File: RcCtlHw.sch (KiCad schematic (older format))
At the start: 28 parts, among them J1 USB_B_Mini, J2 Program, J3 TFT_LCD, SW1 On/Off, U1 TP4056, U2 ESP-M2, U3 ADS1015, U4 Joystick

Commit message: 2nd attempt, looking good
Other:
- note added: "Move SW other side of reg"
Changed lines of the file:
@@
 	1    0    0    -1
 $EndComp
+Text Notes 2300 4650 0    50   ~ 0
+Move SW other side of reg
 $EndSCHEMATC

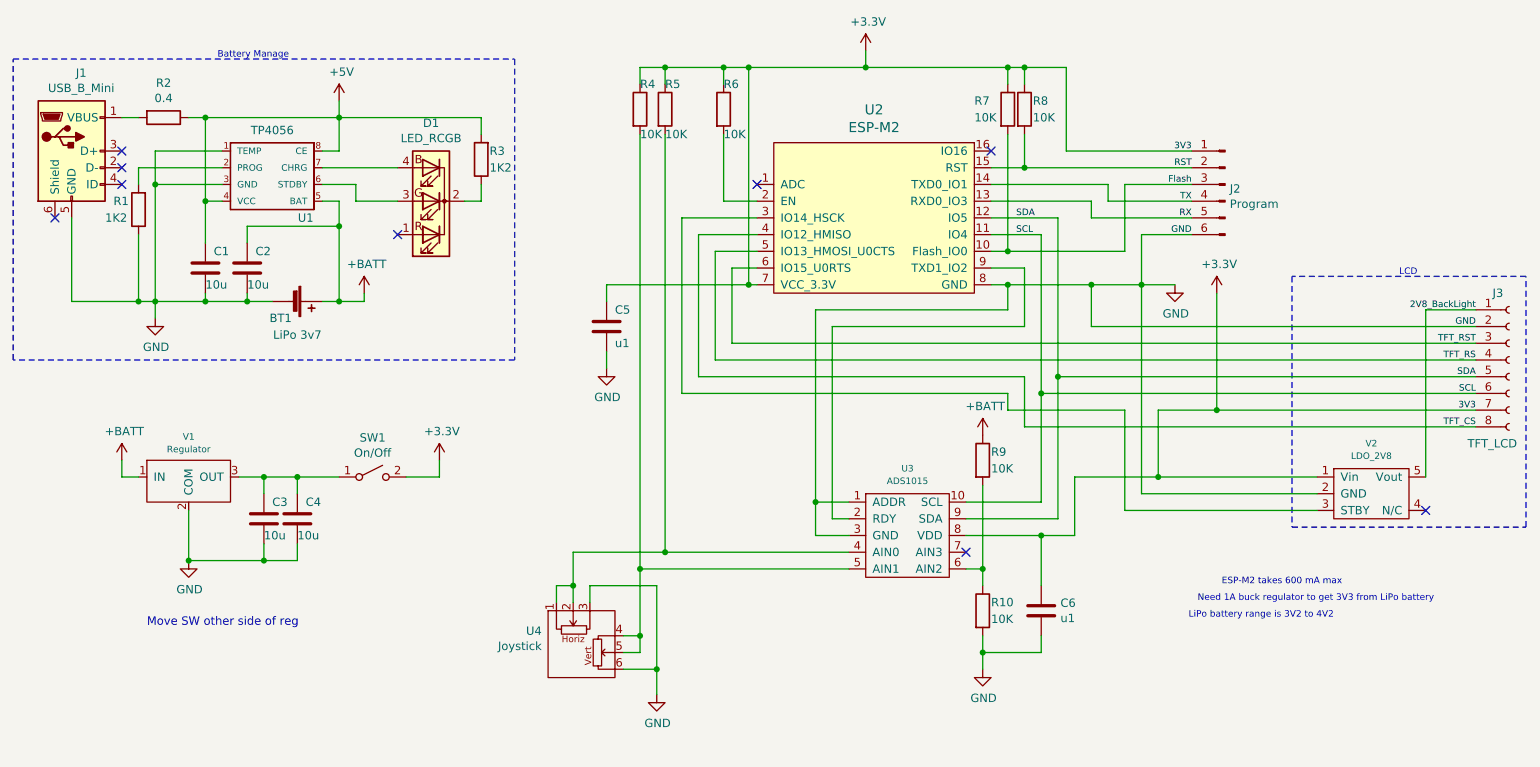
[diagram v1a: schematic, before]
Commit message: Re-Design with big changes for TFT connection
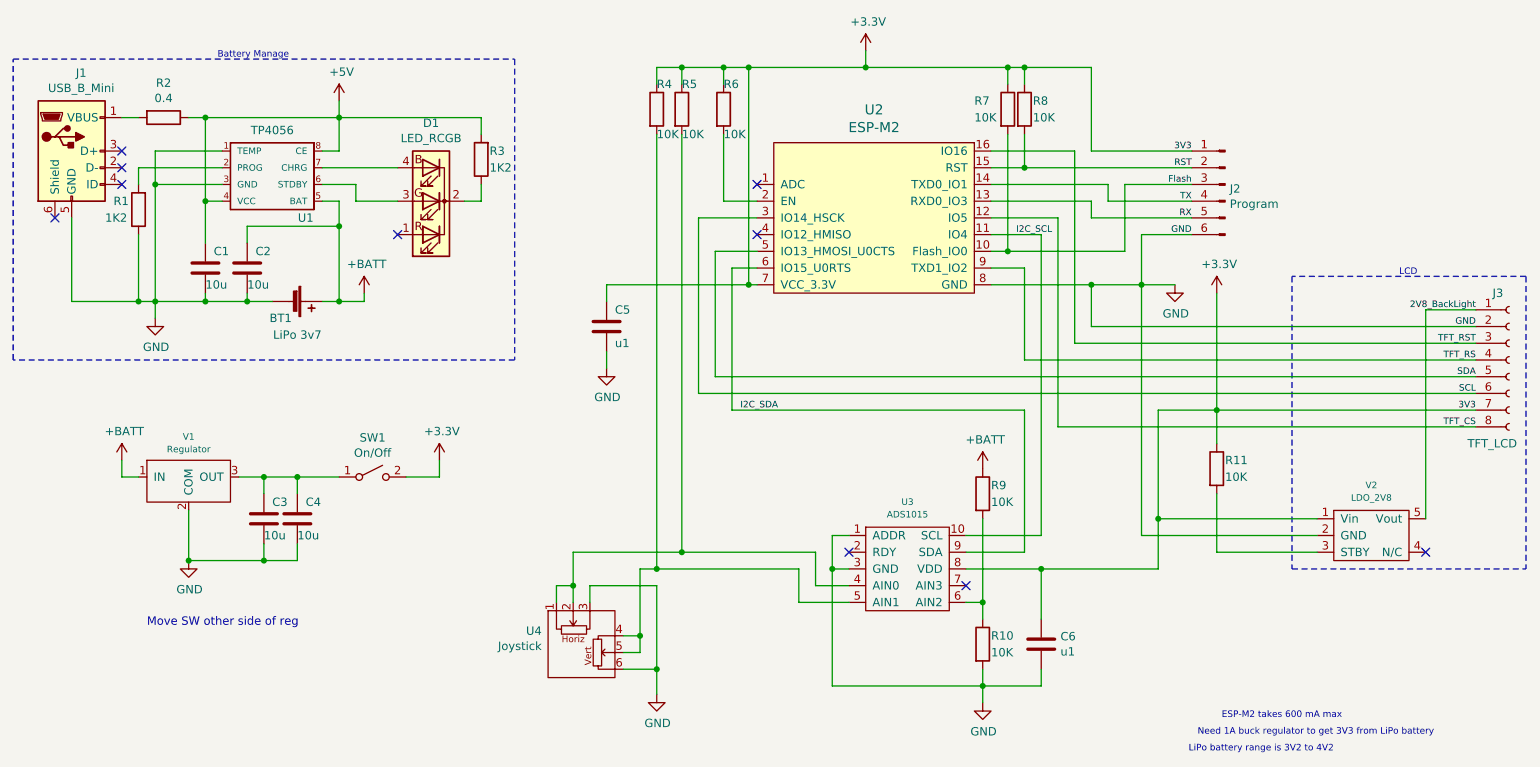
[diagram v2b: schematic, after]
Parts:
- added R11: 10K, Resistor_SMD:R_0805_2012Metric, symbol Device:R
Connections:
- net +3V3: now also R11.1
- net SCL: now also U2.3 (IO14_HSCK); no longer U2.11 (IO4), U3.10 (SCL)
- net SDA: now also U2.5 (IO13_HMOSI_U0CTS); no longer U2.12 (IO5), U3.9 (SDA)
- net TFT_CS: now also U2.12 (IO5); no longer U2.4 (IO12_HMISO)
- net TFT_RS: now also U2.9 (TXD1_IO2); no longer U2.5 (IO13_HMOSI_U0CTS)
- net TFT_RST: now also U2.16 (IO16); no longer U2.6 (IO15_U0RTS)
- net at V2.3 (STBY): now also R11.2; no longer U2.3 (IO14_HSCK)
- net at U3.2 (RDY): no longer U2.9 (TXD1_IO2)
- new net I2C_SCL: U2.11 (IO4), U3.10 (SCL)
- new net I2C_SDA: U2.6 (IO15_U0RTS), U3.9 (SDA)
- no-connect marks 9 -> 10
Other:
- moved on the sheet: C6, R10, R4, R5, R9, U3, V2

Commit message: TFT_CS now connected GND, GPIO5 back to I2C_SDA PCB linked, mostly working USB connector beefed
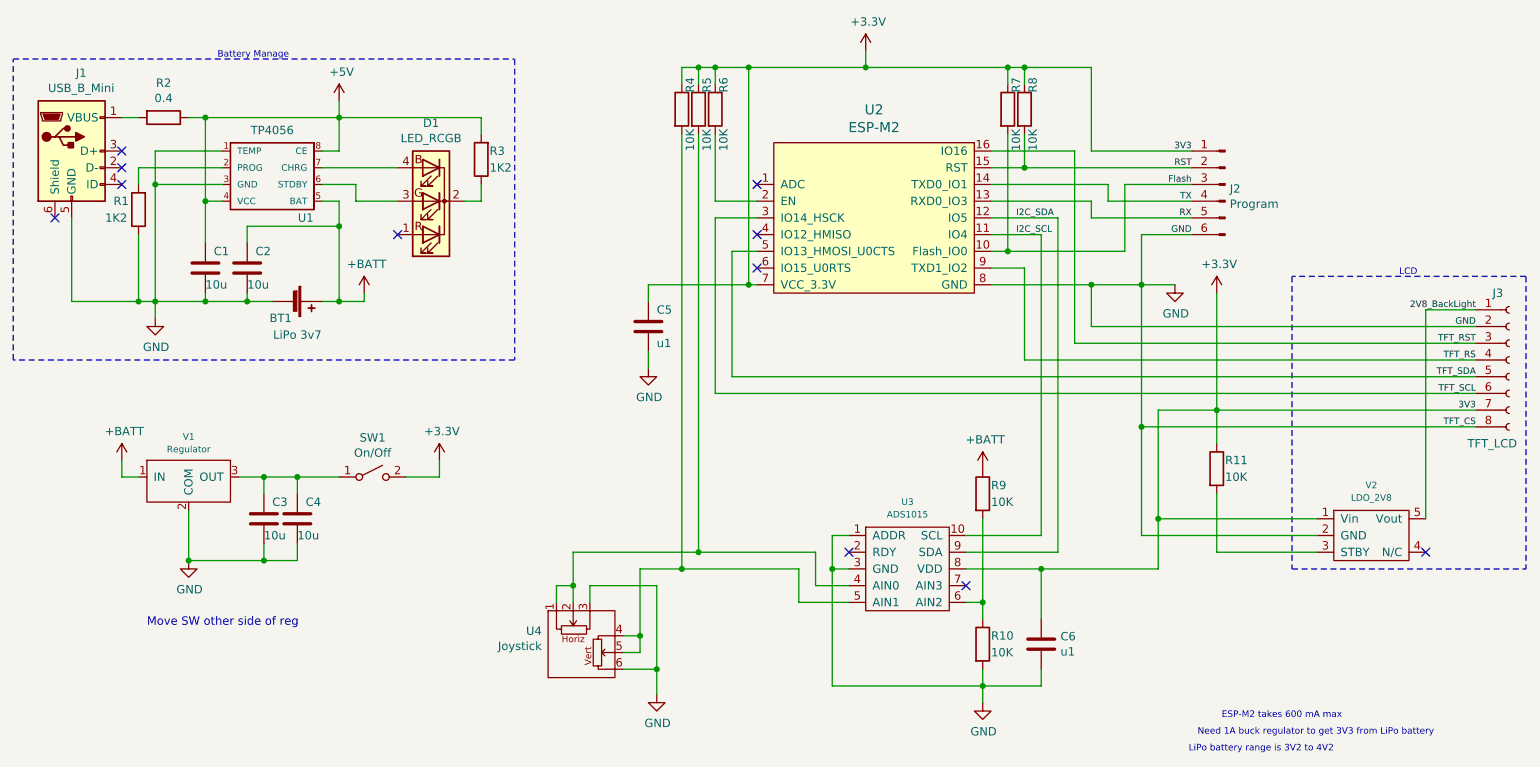
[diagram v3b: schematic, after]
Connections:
- net GND: now also J3.8 (Pin_8)
- net I2C_SDA: now also U2.12 (IO5); no longer U2.6 (IO15_U0RTS)
- net SCL renamed TFT_SCL
- net SDA renamed TFT_SDA
- removed net TFT_CS: J3.8 (Pin_8), U2.12 (IO5)
- no-connect marks 10 -> 11
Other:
- moved on the sheet: C5, R4, R5, R6
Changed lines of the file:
@@
 	4850 4200 4850 4400
 Wire Wire Line
-	5500 4200 4850 4200
+	5600 4200 4850 4200
 Wire Wire Line
 	5250 4700 5250 4800
@@
 Wire Wire Line
 	7200 4100 7650 4100
-Wire Wire Line
-	7200 4200 7550 4200
 Wire Wire Line
 	5150 4800 5250 4800
@@
 Text Notes 9450 5200 2    39   ~ 0
 ESP-M2 takes 600 mA max
-Wire Wire Line
-	5600 2200 5950 2200
-Connection ~ 5750 1300
-Wire Wire Line
-	5500 1300 5750 1300
+Connection ~ 5700 1300
+Wire Wire Line
+	5600 1300 5700 1300
 Connection ~ 5900 2600
 Wire Wire Line
-	5900 2600 5050 2600
+	5900 2600 5300 2600
 Connection ~ 8700 3350
 Wire Wire Line
@@
 Wire Wire Line
 	8700 3350 8700 2650
-Wire Wire Line
-	5700 2400 5950 2400
-Wire Wire Line
-	5800 2500 5950 2500
 Text Label 10250 3450 2    39   ~ 0
 TFT_CS
 Text Label 10250 3250 2    39   ~ 0
-SCL
+TFT_SCL
 Text Label 10250 3150 2    39   ~ 0
-SDA
+TFT_SDA
 Text Label 10250 3050 2    39   ~ 0
 TFT_RS
 Text Label 10250 2950 2    39   ~ 0
 TFT_RST
-Text Label 5850 3350 0    39   ~ 0
+Text Label 7500 2200 0    39   ~ 0
 I2C_SDA
 Text Label 7500 2300 0    39   ~ 0
@@
 	8250 2600 8450 2600
 Wire Wire Line
-	5050 3000 5050 3100
-Wire Wire Line
-	5050 2600 5050 2700
-Wire Wire Line
-	5500 1700 5500 4200
+	5300 3000 5300 3100
+Wire Wire Line
+	5600 1700 5600 4200
 $Comp
 L TrevM:ADS1015 U3
@@
 Text Label 10250 2750 2    39   ~ 0
 2V8_BackLight
-Connection ~ 5500 1300
-Wire Wire Line
-	5500 1300 5350 1300
-Wire Wire Line
-	5500 1300 5500 1400
-Wire Wire Line
-	5750 2100 5950 2100
-Wire Wire Line
-	5750 1700 5750 2100
+Connection ~ 5600 1300
+Wire Wire Line
+	5600 1300 5500 1300
+Wire Wire Line
+	5600 1300 5600 1400
 $Comp
 L Device:R R4
 U 1 1 609528AC
-P 5350 1550
-F 0 "R4" H 5350 1700 50  0000 L CNN
-F 1 "10K" H 5350 1400 50  0000 L CNN
-F 2 "Resistor_SMD:R_0805_2012Metric" V 5280 1550 50  0001 C CNN
-F 3 "~" H 5350 1550 50  0001 C CNN
-	1    5350 1550
-	1    0    0    -1
-$EndComp
-Wire Wire Line
-	5750 1300 5900 1300
-Wire Wire Line
-	5750 1300 5750 1400
-$Comp
-L Device:R R5
-U 1 1 6094C4A2
 P 5500 1550
-F 0 "R5" H 5500 1700 50  0000 L CNN
-F 1 "10K" H 5500 1400 50  0000 L CNN
+F 0 "R4" V 5550 1650 50  0000 L CNN
+F 1 "10K" V 5550 1300 50  0000 L CNN
 F 2 "Resistor_SMD:R_0805_2012Metric" V 5430 1550 50  0001 C CNN
 F 3 "~" H 5500 1550 50  0001 C CNN
 	1    5500 1550
+	1    0    0    -1
+$EndComp
+Wire Wire Line
+	5700 1300 5900 1300
+Wire Wire Line
+	5700 1300 5700 1400
+$Comp
+L Device:R R5
+U 1 1 6094C4A2
+P 5600 1550
+F 0 "R5" V 5650 1650 50  0000 L CNN
+F 1 "10K" V 5650 1300 50  0000 L CNN
+F 2 "Resistor_SMD:R_0805_2012Metric" V 5530 1550 50  0001 C CNN
+F 3 "~" H 5600 1550 50  0001 C CNN
+	1    5600 1550
 	1    0    0    -1
 $EndComp
@@
 L Power:GND #PWR07
 U 1 1 6093378D
-P 5050 3100
-F 0 "#PWR07" H 5050 2850 50  0001 C CNN
-F 1 "GND" H 5055 2927 50  0000 C CNN
-F 2 "" H 5050 3100 50  0001 C CNN
-F 3 "" H 5050 3100 50  0001 C CNN
-	1    5050 3100
+P 5300 3100
+F 0 "#PWR07" H 5300 2850 50  0001 C CNN
+F 1 "GND" H 5305 2927 50  0000 C CNN
+F 2 "" H 5300 3100 50  0001 C CNN
+F 3 "" H 5300 3100 50  0001 C CNN
+	1    5300 3100
 	1    0    0    -1
 $EndComp
@@
 L Device:C C5
 U 1 1 6093070F
-P 5050 2850
-F 0 "C5" H 5100 2950 50  0000 L CNN
-F 1 "u1" H 5100 2750 50  0000 L CNN
-F 2 "Capacitor_SMD:C_0805_2012Metric" H 5088 2700 50  0001 C CNN
-F 3 "~" H 5050 2850 50  0001 C CNN
-	1    5050 2850
+P 5300 2850
+F 0 "C5" H 5350 2950 50  0000 L CNN
+F 1 "u1" H 5350 2750 50  0000 L CNN
+F 2 "Capacitor_SMD:C_0805_2012Metric" H 5338 2700 50  0001 C CNN
+F 3 "~" H 5300 2850 50  0001 C CNN
+	1    5300 2850
 	1    0    0    -1
 $EndComp
@@
 L Device:R R6
 U 1 1 6090CB18
-P 5750 1550
-F 0 "R6" H 5750 1700 50  0000 L CNN
-F 1 "10K" H 5750 1400 50  0000 L CNN
-F 2 "Resistor_SMD:R_0805_2012Metric" V 5680 1550 50  0001 C CNN
-F 3 "~" H 5750 1550 50  0001 C CNN
-	1    5750 1550
+P 5700 1550
+F 0 "R6" V 5750 1650 50  0000 L CNN
+F 1 "10K" V 5750 1300 50  0000 L CNN
+F 2 "Resistor_SMD:R_0805_2012Metric" V 5630 1550 50  0001 C CNN
+F 3 "~" H 5700 1550 50  0001 C CNN
+	1    5700 1550
 	1    0    0    -1
 $EndComp
@@
 U 1 1 6090429E
 P 7550 1550
-F 0 "R8" H 7600 1600 50  0000 L CNN
-F 1 "10K" H 7600 1500 50  0000 L CNN
+F 0 "R8" V 7600 1650 50  0000 L CNN
+F 1 "10K" V 7600 1300 50  0000 L CNN
 F 2 "Resistor_SMD:R_0805_2012Metric" V 7480 1550 50  0001 C CNN
 F 3 "~" H 7550 1550 50  0001 C CNN
@@
 U 1 1 6090119B
 P 7450 1550
-F 0 "R7" H 7250 1600 50  0000 L CNN
-F 1 "10K" H 7250 1500 50  0000 L CNN
+F 0 "R7" V 7500 1650 50  0000 L CNN
+F 1 "10K" V 7500 1300 50  0000 L CNN
 F 2 "Resistor_SMD:R_0805_2012Metric" V 7380 1550 50  0001 C CNN
 F 3 "~" H 7450 1550 50  0001 C CNN
@@
 $EndComp
 Wire Wire Line
-	8250 2600 8250 4100
+	8250 2600 8250 3450
 Wire Wire Line
 	9300 4200 8700 4200
@@
 	7550 2500 7550 3050
 Wire Wire Line
-	10250 3150 5700 3150
-Wire Wire Line
-	5700 2400 5700 3150
-Wire Wire Line
-	10250 3250 5600 3250
-Wire Wire Line
-	5600 3250 5600 2200
+	10250 3150 5800 3150
+Wire Wire Line
+	10250 3250 5700 3250
 NoConn ~ 6500 4200
-Wire Wire Line
-	10250 3450 7750 3450
-Wire Wire Line
-	7750 3450 7750 2200
-Wire Wire Line
-	7750 2200 7350 2200
 Wire Wire Line
 	6500 4300 6400 4300
@@
 	8350 3350 8350 4000
 Wire Wire Line
-	5500 4200 6300 4200
+	5600 4200 6300 4200
 Wire Wire Line
 	6300 4200 6300 4400
-Connection ~ 5500 4200
+Connection ~ 5600 4200
 Wire Wire Line
 	6300 4400 6500 4400
 Wire Wire Line
-	5250 4300 5350 4300
+	5250 4300 5500 4300
 Wire Wire Line
 	6200 4300 6200 4500
@@
 Wire Wire Line
 	5250 4300 5250 4700
-Wire Wire Line
-	7550 4200 7550 3350
-Wire Wire Line
-	7550 3350 5800 3350
-Wire Wire Line
-	5800 3350 5800 2500
 Wire Wire Line
 	7650 2300 7650 4100
@@
 	7350 2600 7950 2600
 NoConn ~ 5950 2300
-Wire Wire Line
-	5350 1400 5350 1300
-Connection ~ 5350 4300
-Wire Wire Line
-	5350 4300 6200 4300
-Wire Wire Line
-	5350 1700 5350 4300
+Connection ~ 5500 4300
+Wire Wire Line
+	5500 4300 6200 4300
+Wire Wire Line
+	5500 1700 5500 4300
+Wire Wire Line
+	10250 3450 8250 3450
+Connection ~ 8250 3450
+Wire Wire Line
+	8250 3450 8250 4100
+Wire Wire Line
+	7750 4200 7750 2200
+Wire Wire Line
+	7750 2200 7350 2200
+Wire Wire Line
+	7200 4200 7750 4200
+NoConn ~ 5950 2500
+Wire Wire Line
+	5800 2400 5800 3150
+Wire Wire Line
+	5800 2400 5950 2400
+Wire Wire Line
+	5700 2200 5700 3250
+Wire Wire Line
+	5700 2200 5950 2200
+Wire Wire Line
+	5700 1700 5700 2100
+Wire Wire Line
+	5700 2100 5950 2100
+Wire Wire Line
+	5500 1400 5500 1300
+Wire Wire Line
+	5300 2700 5300 2600
 $EndSCHEMATC

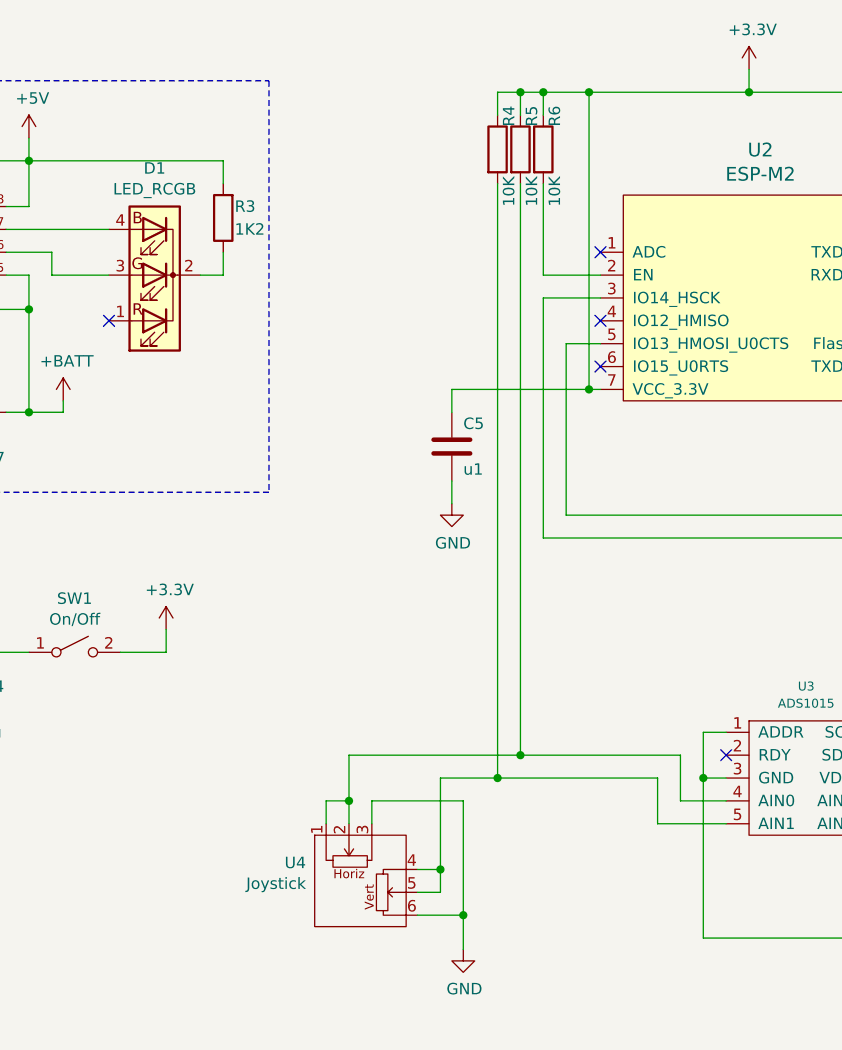
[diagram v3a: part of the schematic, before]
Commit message: beefed up USB connector mountings, joystick now swings GND to 3V3 on H & V
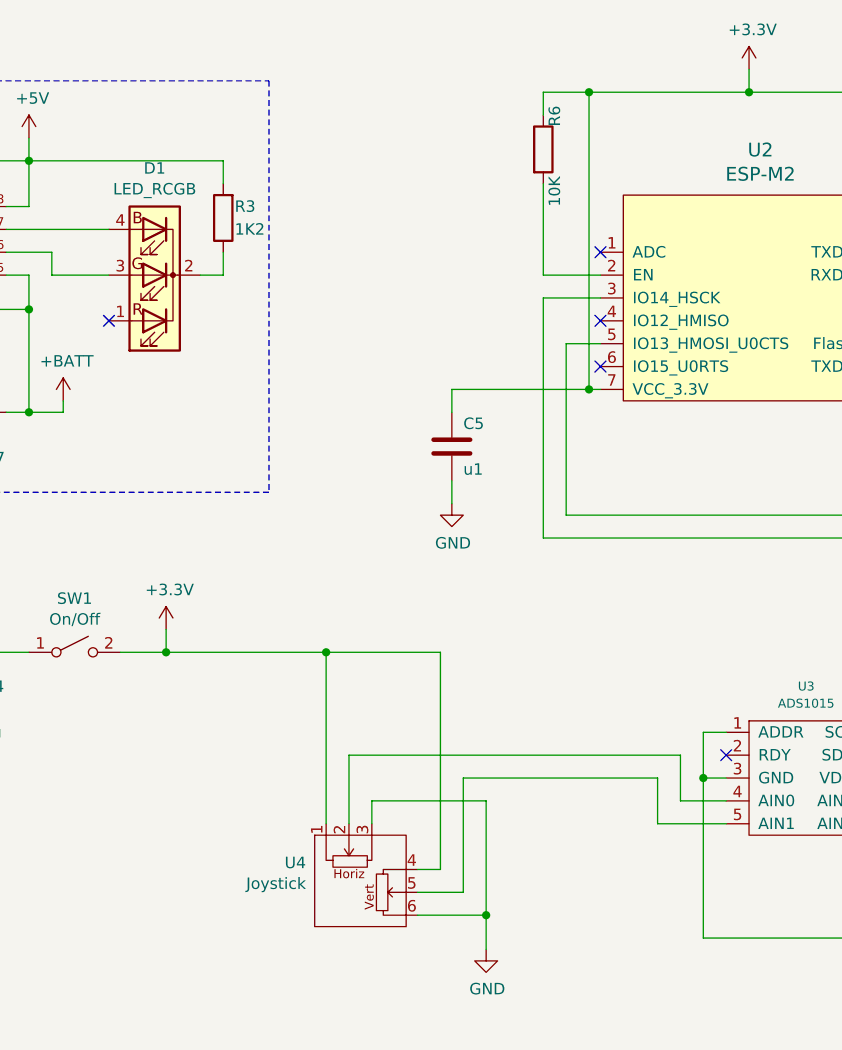
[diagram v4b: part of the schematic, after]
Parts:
- removed R4, R5: 10K, Resistor_SMD:R_0805_2012Metric, symbol Device:R
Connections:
- net +3V3: now also U4.1, U4.4
- net at U3.4 (AIN0), U4.2: no longer U4.1
- net at U3.5 (AIN1), U4.5: no longer U4.4
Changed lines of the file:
@@
 Wire Wire Line
 	7300 4900 7300 5000
-Connection ~ 4850 4400
-Wire Wire Line
-	4850 4200 4850 4400
-Wire Wire Line
-	5600 4200 4850 4200
-Wire Wire Line
-	5250 4700 5250 4800
-Connection ~ 5250 4700
-Wire Wire Line
-	5150 4700 5250 4700
 Wire Wire Line
 	4950 4400 4950 4500
 Wire Wire Line
-	4850 4400 4850 4500
-Wire Wire Line
-	4750 4500 4750 4400
-Wire Wire Line
-	4750 4400 4850 4400
-Wire Wire Line
-	4950 4400 5350 4400
+	4950 4400 5450 4400
 Wire Wire Line
 	7200 4100 7650 4100
 Wire Wire Line
-	5150 4800 5250 4800
+	5150 4800 5350 4800
 Wire Wire Line
 	6500 4100 6400 4100
@@
 $EndComp
 Wire Wire Line
-	5350 4900 5350 5050
-Connection ~ 5350 4900
-Wire Wire Line
-	5150 4900 5350 4900
-Wire Wire Line
-	5350 4400 5350 4900
+	5450 4900 5450 5050
+Connection ~ 5450 4900
+Wire Wire Line
+	5150 4900 5450 4900
+Wire Wire Line
+	5450 4400 5450 4900
 $Comp
 L TrevM:Joystick U4
@@
 Text Notes 9450 5200 2    39   ~ 0
 ESP-M2 takes 600 mA max
-Connection ~ 5700 1300
-Wire Wire Line
-	5600 1300 5700 1300
 Connection ~ 5900 2600
 Wire Wire Line
@@
 Wire Wire Line
 	5300 3000 5300 3100
-Wire Wire Line
-	5600 1700 5600 4200
 $Comp
 L TrevM:ADS1015 U3
@@
 Text Label 10250 2750 2    39   ~ 0
 2V8_BackLight
-Connection ~ 5600 1300
-Wire Wire Line
-	5600 1300 5500 1300
-Wire Wire Line
-	5600 1300 5600 1400
-$Comp
-L Device:R R4
-U 1 1 609528AC
-P 5500 1550
-F 0 "R4" V 5550 1650 50  0000 L CNN
-F 1 "10K" V 5550 1300 50  0000 L CNN
-F 2 "Resistor_SMD:R_0805_2012Metric" V 5430 1550 50  0001 C CNN
-F 3 "~" H 5500 1550 50  0001 C CNN
-	1    5500 1550
-	1    0    0    -1
-$EndComp
 Wire Wire Line
 	5700 1300 5900 1300
 Wire Wire Line
 	5700 1300 5700 1400
-$Comp
-L Device:R R5
-U 1 1 6094C4A2
-P 5600 1550
-F 0 "R5" V 5650 1650 50  0000 L CNN
-F 1 "10K" V 5650 1300 50  0000 L CNN
-F 2 "Resistor_SMD:R_0805_2012Metric" V 5530 1550 50  0001 C CNN
-F 3 "~" H 5600 1550 50  0001 C CNN
-	1    5600 1550
-	1    0    0    -1
-$EndComp
 $Comp
 L Power:GND #PWR09
 U 1 1 6093A1CB
-P 5350 5050
-F 0 "#PWR09" H 5350 4800 50  0001 C CNN
-F 1 "GND" H 5355 4877 50  0000 C CNN
-F 2 "" H 5350 5050 50  0001 C CNN
-F 3 "" H 5350 5050 50  0001 C CNN
-	1    5350 5050
+P 5450 5050
+F 0 "#PWR09" H 5450 4800 50  0001 C CNN
+F 1 "GND" H 5455 4877 50  0000 C CNN
+F 2 "" H 5450 5050 50  0001 C CNN
+F 3 "" H 5450 5050 50  0001 C CNN
+	1    5450 5050
 	1    0    0    -1
 $EndComp
@@
 	8350 3350 8350 4000
 Wire Wire Line
-	5600 4200 6300 4200
-Wire Wire Line
 	6300 4200 6300 4400
-Connection ~ 5600 4200
 Wire Wire Line
 	6300 4400 6500 4400
 Wire Wire Line
-	5250 4300 5500 4300
-Wire Wire Line
 	6200 4300 6200 4500
 Wire Wire Line
 	6200 4500 6500 4500
-Wire Wire Line
-	5250 4300 5250 4700
 Wire Wire Line
 	7650 2300 7650 4100
@@
 	7350 2600 7950 2600
 NoConn ~ 5950 2300
-Connection ~ 5500 4300
-Wire Wire Line
-	5500 4300 6200 4300
-Wire Wire Line
-	5500 1700 5500 4300
 Wire Wire Line
 	10250 3450 8250 3450
@@
 	5700 2100 5950 2100
 Wire Wire Line
-	5500 1400 5500 1300
-Wire Wire Line
 	5300 2700 5300 2600
+Wire Wire Line
+	4850 4200 6300 4200
+Wire Wire Line
+	5350 4300 6200 4300
+Wire Wire Line
+	4850 4200 4850 4500
+Wire Wire Line
+	5350 4300 5350 4800
+Wire Wire Line
+	4050 3750 4750 3750
+Wire Wire Line
+	4750 3750 4750 4500
+Connection ~ 4050 3750
+Wire Wire Line
+	5150 4700 5250 4700
+Wire Wire Line
+	5250 4700 5250 3750
+Wire Wire Line
+	5250 3750 4750 3750
+Connection ~ 4750 3750
 $EndSCHEMATC
